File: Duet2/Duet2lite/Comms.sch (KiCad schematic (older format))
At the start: 42 parts, among them J15 uSDHC, J22 USB, U12 74HC74, U4 ESP-07/12

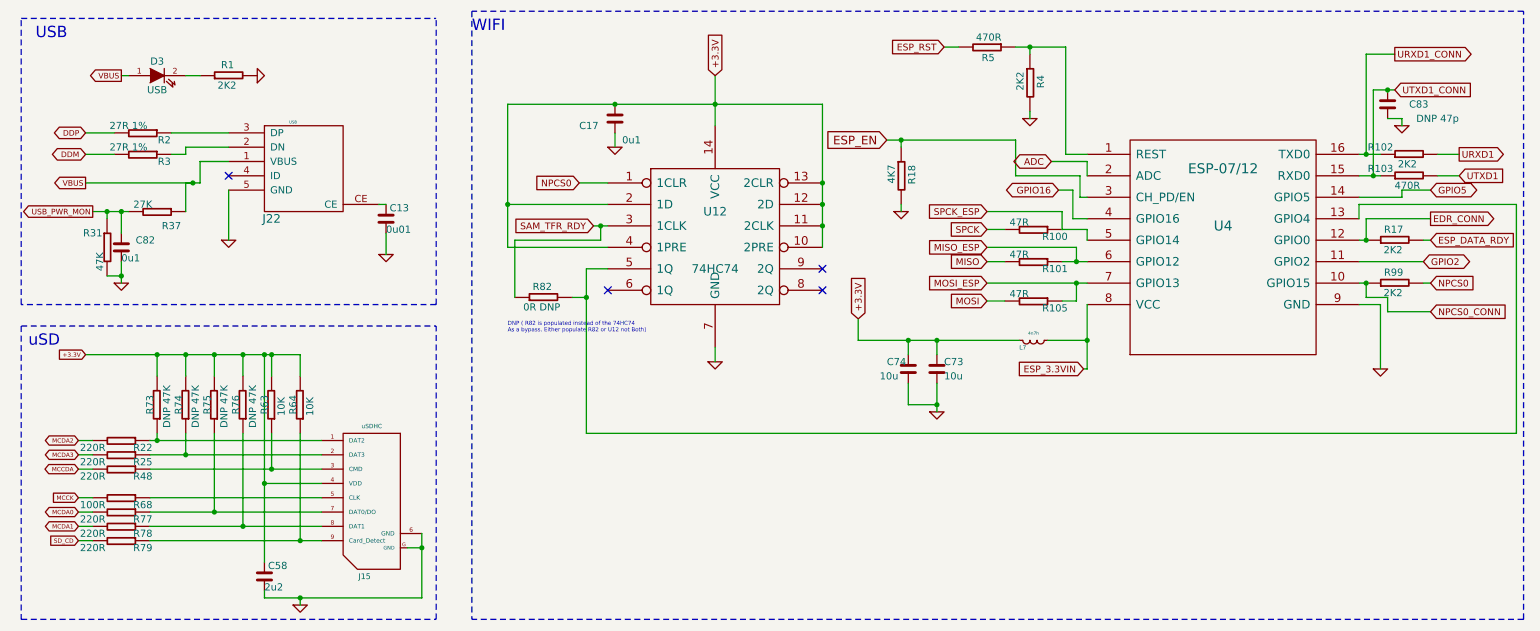
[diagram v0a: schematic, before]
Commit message: removed stepper drivers from the schematic
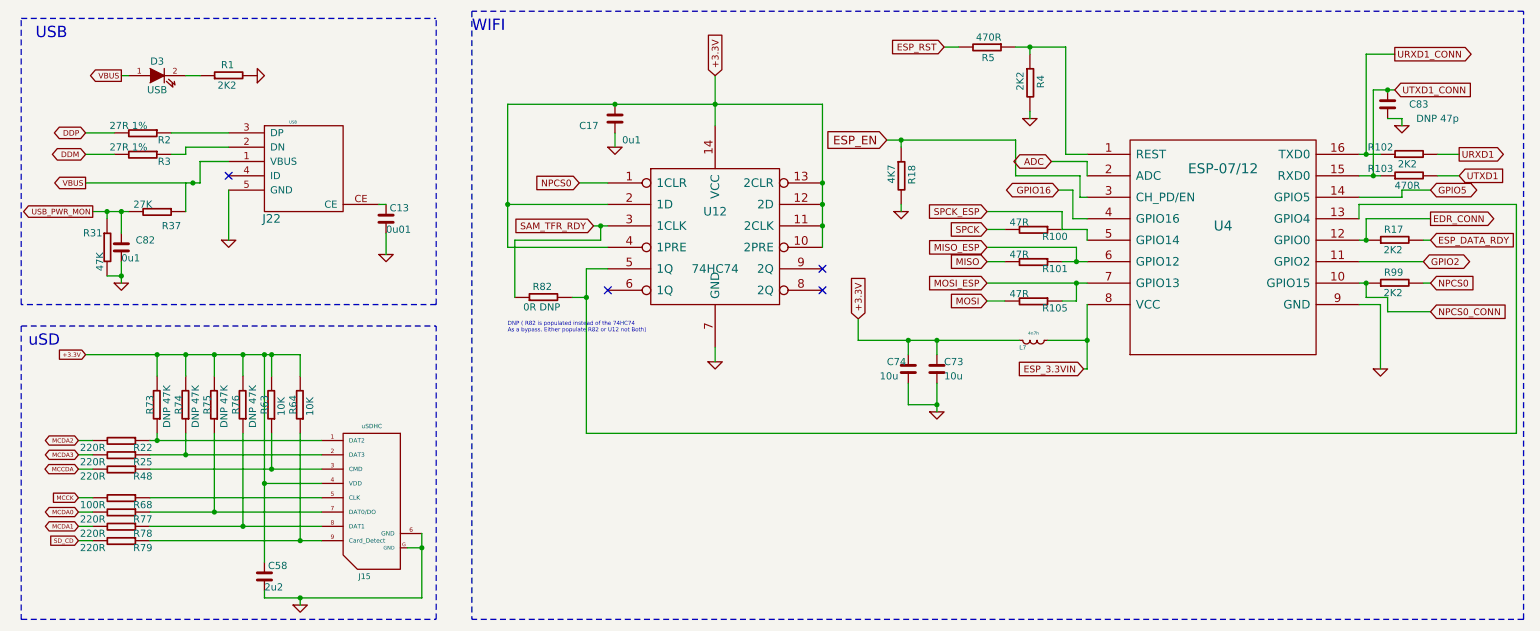
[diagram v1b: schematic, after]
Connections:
- net VBUS: no longer R37.1
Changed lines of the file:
@@
 P 3200 2250
 AR Path="/53B18095" Ref="#PWR041"  Part="1"
-AR Path="/50577C6A/53B18095" Ref="#PWR69"  Part="1"
-F 0 "#PWR69" H 3200 2250 30  0001 C CNN
+AR Path="/50577C6A/53B18095" Ref="#PWR069"  Part="1"
+F 0 "#PWR069" H 3200 2250 30  0001 C CNN
 F 1 "GND" H 3200 2180 30  0001 C CNN
 F 2 "" H 3200 2250 60  0001 C CNN
@@
 P 2300 1000
 AR Path="/50F1BB8D" Ref="#PWR042"  Part="1"
-AR Path="/50577C6A/50F1BB8D" Ref="#PWR67"  Part="1"
-F 0 "#PWR67" H 2300 1000 30  0001 C CNN
+AR Path="/50577C6A/50F1BB8D" Ref="#PWR067"  Part="1"
+F 0 "#PWR067" H 2300 1000 30  0001 C CNN
 F 1 "GND" H 2300 930 30  0001 C CNN
 F 2 "" H 2300 1000 60  0001 C CNN
@@
 P 2600 4700
 AR Path="/505F7C09" Ref="#PWR043"  Part="1"
-AR Path="/50577C6A/505F7C09" Ref="#PWR68"  Part="1"
-F 0 "#PWR68" H 2600 4700 30  0001 C CNN
+AR Path="/50577C6A/505F7C09" Ref="#PWR068"  Part="1"
+F 0 "#PWR068" H 2600 4700 30  0001 C CNN
 F 1 "GND" H 2600 4630 30  0001 C CNN
 F 2 "" H 2600 4700 60  0001 C CNN
@@
 P 2100 2150
 AR Path="/505F6D36" Ref="#PWR044"  Part="1"
-AR Path="/50577C6A/505F6D36" Ref="#PWR66"  Part="1"
-F 0 "#PWR66" H 2100 2150 30  0001 C CNN
+AR Path="/50577C6A/505F6D36" Ref="#PWR066"  Part="1"
+F 0 "#PWR066" H 2100 2150 30  0001 C CNN
 F 1 "GND" H 2100 2080 30  0001 C CNN
 F 2 "" H 2100 2150 60  0001 C CNN
@@
 P 7700 1300
 AR Path="/568407A1" Ref="#PWR045"  Part="1"
-AR Path="/50577C6A/568407A1" Ref="#PWR74"  Part="1"
-F 0 "#PWR74" H 7700 1300 30  0001 C CNN
+AR Path="/50577C6A/568407A1" Ref="#PWR074"  Part="1"
+F 0 "#PWR074" H 7700 1300 30  0001 C CNN
 F 1 "GND" H 7700 1230 30  0001 C CNN
 F 2 "" H 7700 1300 60  0001 C CNN
@@
 P 10150 3050
 AR Path="/56840A06" Ref="#PWR046"  Part="1"
-AR Path="/50577C6A/56840A06" Ref="#PWR75"  Part="1"
-F 0 "#PWR75" H 10150 3050 30  0001 C CNN
+AR Path="/50577C6A/56840A06" Ref="#PWR075"  Part="1"
+F 0 "#PWR075" H 10150 3050 30  0001 C CNN
 F 1 "GND" H 10150 2980 30  0001 C CNN
 F 2 "" H 10150 3050 60  0001 C CNN
@@
 P 5500 3000
 AR Path="/568495D3" Ref="#PWR047"  Part="1"
-AR Path="/50577C6A/568495D3" Ref="#PWR71"  Part="1"
-F 0 "#PWR71" H 5500 3000 30  0001 C CNN
+AR Path="/50577C6A/568495D3" Ref="#PWR071"  Part="1"
+F 0 "#PWR071" H 5500 3000 30  0001 C CNN
 F 1 "GND" H 5500 2930 30  0001 C CNN
 F 2 "" H 5500 3000 60  0001 C CNN
@@
 P 7050 3350
 AR Path="/5688FD9E" Ref="#PWR048"  Part="1"
-AR Path="/50577C6A/5688FD9E" Ref="#PWR73"  Part="1"
-F 0 "#PWR73" H 7050 3350 30  0001 C CNN
+AR Path="/50577C6A/5688FD9E" Ref="#PWR073"  Part="1"
+F 0 "#PWR073" H 7050 3350 30  0001 C CNN
 F 1 "GND" H 7050 3280 30  0001 C CNN
 F 2 "" H 7050 3350 60  0001 C CNN
@@
 P 6800 1950
 AR Path="/56943A84" Ref="#PWR049"  Part="1"
-AR Path="/50577C6A/56943A84" Ref="#PWR72"  Part="1"
-F 0 "#PWR72" H 6800 1950 30  0001 C CNN
+AR Path="/50577C6A/56943A84" Ref="#PWR072"  Part="1"
+F 0 "#PWR072" H 6800 1950 30  0001 C CNN
 F 1 "GND" H 6800 1880 30  0001 C CNN
 F 2 "" H 6800 1950 60  0001 C CNN
@@
 P 4800 1500
 AR Path="/56943B32" Ref="#PWR050"  Part="1"
-AR Path="/50577C6A/56943B32" Ref="#PWR70"  Part="1"
-F 0 "#PWR70" H 4800 1500 30  0001 C CNN
+AR Path="/50577C6A/56943B32" Ref="#PWR070"  Part="1"
+F 0 "#PWR070" H 4800 1500 30  0001 C CNN
 F 1 "GND" H 4800 1430 30  0001 C CNN
 F 2 "" H 4800 1500 60  0001 C CNN
@@
 P 1350 2450
 AR Path="/5706BFDA" Ref="#PWR051"  Part="1"
-AR Path="/50577C6A/5706BFDA" Ref="#PWR65"  Part="1"
-F 0 "#PWR65" H 1350 2450 30  0001 C CNN
+AR Path="/50577C6A/5706BFDA" Ref="#PWR065"  Part="1"
+F 0 "#PWR065" H 1350 2450 30  0001 C CNN
 F 1 "GND" H 1350 2380 30  0001 C CNN
 F 2 "" H 1350 2450 60  0001 C CNN
@@
 P 10300 1350
 AR Path="/5719E79B" Ref="#PWR052"  Part="1"
-AR Path="/50577C6A/5719E79B" Ref="#PWR76"  Part="1"
-F 0 "#PWR76" H 10300 1350 30  0001 C CNN
+AR Path="/50577C6A/5719E79B" Ref="#PWR076"  Part="1"
+F 0 "#PWR076" H 10300 1350 30  0001 C CNN
 F 1 "GND" H 10300 1280 30  0001 C CNN
 F 2 "" H 10300 1350 60  0001 C CNN
@@
 Connection ~ 3450 4300
 Wire Wire Line
-	3450 4650 3450 4200
-Wire Wire Line
-	2350 4650 3450 4650
+	3450 4650 3450 4300
+Wire Wire Line
+	2350 4650 2600 4650
 Wire Notes Line
 	3550 2600 650  2600
@@
 	3800 550  3800 4800
 Wire Wire Line
-	1900 1750 1100 1750
-Wire Wire Line
 	1100 1400 1300 1400
 Wire Wire Line
@@
 	3350 4300 3450 4300
 Wire Wire Line
-	2350 2950 2350 4400
+	2350 2950 2350 3850
 Wire Wire Line
 	2000 2950 2000 3100
@@
 	7700 1300 7700 1250
 Wire Wire Line
-	7600 800  7950 800
-Wire Wire Line
-	10000 1550 10150 1550
-Wire Wire Line
-	10000 1700 10150 1700
+	7600 800  7700 800
+Wire Wire Line
+	10000 1550 10050 1550
+Wire Wire Line
+	10000 1700 10100 1700
 Wire Wire Line
 	6500 2700 6500 2850
@@
 	5500 2900 5500 3000
 Wire Wire Line
-	5500 1000 5500 1350
-Wire Wire Line
-	7925 2300 8100 2300
-Wire Wire Line
-	6700 1450 7600 1450
+	5500 1000 5500 1200
+Wire Wire Line
+	7925 2300 8025 2300
+Wire Wire Line
+	6700 1450 6800 1450
 Wire Wire Line
 	8100 1550 7950 1550
@@
 	7950 1550 7950 800
 Wire Wire Line
-	7050 3150 7050 3350
+	7050 3150 7050 3300
 Wire Wire Line
 	4550 1750 4750 1750
@@
 	4050 2200 4750 2200
 Wire Wire Line
-	4050 1200 4050 2200
-Wire Wire Line
-	4650 2050 4750 2050
+	4050 1200 4050 1900
+Wire Wire Line
+	4650 2050 4700 2050
 Wire Wire Line
 	4750 1900 4050 1900
 Connection ~ 4050 1900
 Wire Wire Line
-	6250 1200 6250 2200
+	6250 1200 6250 1750
 Connection ~ 6250 2050
 Connection ~ 6250 1900
@@
 	4750 2350 4600 2350
 Wire Wire Line
-	4600 2350 4600 3500
+	4600 2350 4600 2550
 Wire Wire Line
 	4600 3500 11100 3500
@@
 	1050 3650 1150 3650
 Wire Wire Line
-	1550 3750 2750 3750
+	1550 3750 2400 3750
 Wire Wire Line
 	1050 3950 1150 3950
@@
 	1550 3950 2750 3950
 Wire Wire Line
-	1550 4250 2750 4250
+	1550 4250 2600 4250
 Wire Wire Line
 	1150 3550 1050 3550
 Wire Wire Line
-	1550 3550 2750 3550
+	1550 3550 1600 3550
 Wire Wire Line
 	1600 3550 1600 3500
@@
 	2750 3850 2350 3850
 Wire Wire Line
-	1550 4050 2750 4050
+	1550 4050 2000 4050
 Wire Wire Line
 	2000 4050 2000 3500
 Connection ~ 2000 4050
 Wire Wire Line
-	1550 4150 2750 4150
+	1550 4150 2200 4150
 Wire Wire Line
 	2200 4150 2200 3500
@@
 	1050 4250 1150 4250
 Wire Wire Line
-	1550 3650 2750 3650
+	1550 3650 1800 3650
 Wire Wire Line
 	1800 3650 1800 3500
 Connection ~ 1800 3650
 Wire Wire Line
-	1100 2950 2600 2950
+	1100 2950 1600 2950
 Wire Wire Line
 	2400 2950 2400 3100
@@
 	4800 1400 4800 1500
 Wire Wire Line
-	4050 1200 6250 1200
+	4050 1200 4800 1200
 Connection ~ 5500 1200
 Connection ~ 4800 1200
@@
 Connection ~ 10050 1550
 Wire Wire Line
-	10100 1100 10250 1100
+	10100 1100 10200 1100
 Wire Wire Line
 	6850 2950 6850 2850
@@
 	6850 3150 6850 3300
 Wire Wire Line
-	1850 1750 1800 1750
-Wire Wire Line
 	1800 1750 1800 1950
 Connection ~ 1850 1750
 Wire Wire Line
-	1350 2300 1350 2450
+	1350 2300 1350 2400
 Wire Wire Line
 	1350 2400 1250 2400
@@
 	1350 1950 1350 2100
 Wire Wire Line
-	1150 1950 1400 1950
+	1150 1950 1250 1950
 Wire Wire Line
 	1250 2000 1250 1950
@@
 	7525 2575 7400 2575
 Wire Wire Line
-	6500 2850 7625 2850
+	6500 2850 6850 2850
 Wire Wire Line
 	7825 2850 8100 2850
@@
 	8025 2575 8025 2450
 Wire Wire Line
-	7400 2450 8100 2450
+	7400 2450 8025 2450
 Connection ~ 8025 2450
 Text GLabel 7400 2200 0    47   Input ~ 0
@@
 	8100 3050 8075 3050
 Wire Wire Line
-	8100 2600 8100 3050
+	8100 2600 8100 2850
+Wire Wire Line
+	1800 2950 2000 2950
+Wire Wire Line
+	2200 2950 2350 2950
+Wire Wire Line
+	2350 3850 2350 4400
+Wire Wire Line
+	3450 4300 3450 4200
+Wire Wire Line
+	2600 4650 3450 4650
+Wire Wire Line
+	2000 2950 2200 2950
+Wire Wire Line
+	1600 2950 1800 2950
+Wire Wire Line
+	4050 1900 4050 2200
+Wire Wire Line
+	6250 2050 6250 2200
+Wire Wire Line
+	6250 1900 6250 2050
+Wire Wire Line
+	6250 1750 6250 1900
+Wire Wire Line
+	1600 3550 2750 3550
+Wire Wire Line
+	2000 4050 2750 4050
+Wire Wire Line
+	2200 4150 2750 4150
+Wire Wire Line
+	1800 3650 2750 3650
+Wire Wire Line
+	2350 2950 2400 2950
+Wire Wire Line
+	2400 2950 2600 2950
+Wire Wire Line
+	2400 3750 2750 3750
+Wire Wire Line
+	2600 4250 2750 4250
+Wire Wire Line
+	7700 800  7950 800
+Wire Wire Line
+	6800 1450 7600 1450
+Wire Wire Line
+	5500 1200 5500 1350
+Wire Wire Line
+	5500 1200 6250 1200
+Wire Wire Line
+	4800 1200 5500 1200
+Wire Wire Line
+	4700 2050 4750 2050
+Wire Wire Line
+	4600 2550 4600 3500
+Wire Wire Line
+	7050 2850 7625 2850
+Wire Wire Line
+	7050 3300 7050 3350
+Wire Wire Line
+	10100 1700 10150 1700
+Wire Wire Line
+	10050 1550 10150 1550
+Wire Wire Line
+	6850 2850 7050 2850
+Wire Wire Line
+	1350 2400 1350 2450
+Wire Wire Line
+	1350 1950 1400 1950
+Wire Wire Line
+	1250 1950 1350 1950
+Wire Wire Line
+	10200 1100 10250 1100
+Wire Wire Line
+	8025 2450 8100 2450
+Wire Wire Line
+	8025 2300 8100 2300
+Wire Wire Line
+	8100 2850 8100 3050
+Wire Wire Line
+	1100 1750 1900 1750
 $EndSCHEMATC
